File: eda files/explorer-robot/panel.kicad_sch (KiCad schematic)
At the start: 15 parts, among them J11 PANEL.BUS, J12 PANEL.CTRL, U11 TPS22917DBV

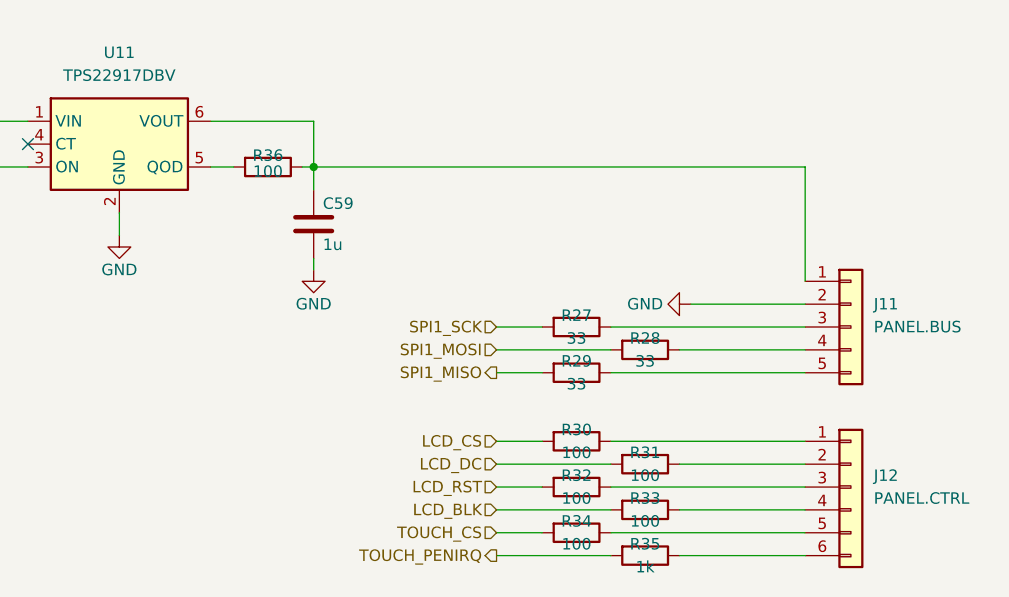
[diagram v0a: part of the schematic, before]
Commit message: ``` Move AI camera branch to 3.3 V rail
The Grove Vision AI V2 module used here requires a 3.3 V input,
so powering it from the switched 5 V branch would over-voltage it.
Point U9 VIN at +3.3V; the TPS22917, footprint and control are
unchanged.

Also bump the 5 V inductor to 15 µH/3 A, swap the catch diode,
clean up schematic wiring and add no-connects on unused pins.
Document the decision in ADR-0025 and update ADR-0019, ADR-0021
and CONTEXT.md.
```
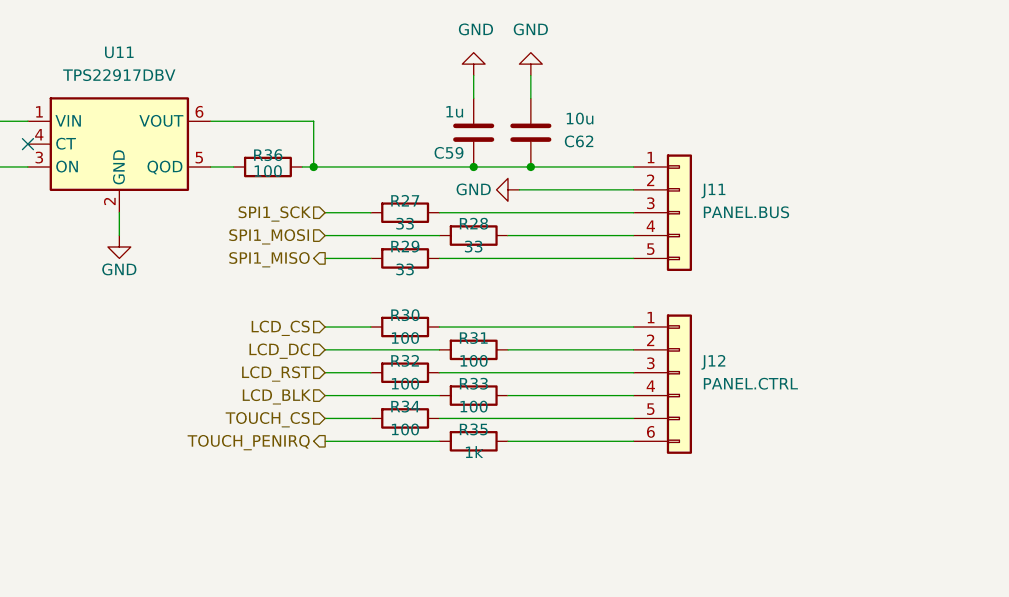
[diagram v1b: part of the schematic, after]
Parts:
- added C62: 10u, Capacitor_SMD:C_0805_2012Metric, symbol Device:C
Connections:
- net GND: now also C62.2
- net at C59.1, J11.1 (Pin_1), R36.1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: now also C62.1
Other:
- moved on the sheet: J11, J12, R27, R28, R29, R30, R31, R32, R33, R34, R35

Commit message: place test points, tidy up, ERC
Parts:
- added TP20: T.TCH.PEN, Connector_PinHeader_2.54mm:PinHeader_1x02_P2.54mm_Vertical, symbol Connector:TestPoint_2Pole
- added TP21: T.TCH.CS, Connector_PinHeader_2.54mm:PinHeader_1x02_P2.54mm_Vertical, symbol Connector:TestPoint_2Pole
- added TP22: T.LCD.CS, Connector_PinHeader_2.54mm:PinHeader_1x02_P2.54mm_Vertical, symbol Connector:TestPoint_2Pole
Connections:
- net GND: now also TP20.1, TP21.1, TP22.1
- net LCD_CS: now also TP22.2
- net TOUCH_CS: now also TP21.2
- net TOUCH_PENIRQ: now also TP20.2
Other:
- note added: "Test Points"

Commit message: Add LCSC part metadata to explorer-robot schematics
Populate JLCPCB_URL, LCSC, MPN, and MFR fields on components in the
panel and rangefinder sheets, and default the BOM view to sort by
LCSC ascending. Rename TB6612FNG test points to match motor encoder
nets, adjust their placement, and drop two symbols from the BOM and
position files.
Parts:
- R27, R28, R29: JLCPCB_URL (none) -> https://jlcpcb.com/partdetail/23867-0603WAF330JT5E/C23140; LCSC (none) -> C23140; MPN (none) -> 0603WAF330JT5E
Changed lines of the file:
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@@
+			)
+		)
+		(property "JLCPCB_URL" "https://jlcpcb.com/partdetail/23867-0603WAF330JT5E/C23140"
+			(at 157.48 85.09 90)
+			(hide yes)
+			(show_name no)
+			(do_not_autoplace no)
+			(effects
+				(font
+					(size 1.27 1.27)
+				)
+			)
+		)
+		(property "LCSC" "C23140"
+			(at 157.48 85.09 90)
+			(hide yes)
+			(show_name no)
+			(do_not_autoplace no)
+			(effects
+				(font
+					(size 1.27 1.27)
+				)
+			)
+		)
+		(property "MPN" "0603WAF330JT5E"
+			(at 157.48 85.09 90)
+			(hide yes)
+			(show_name no)
+			(do_not_autoplace no)
+			(effects
+				(font
+					(size 1.27 1.27)
+				)
 			)
 		)
@@
 			)
 		)
+		(property "JLCPCB_URL" "https://jlcpcb.com/partdetail/23867-0603WAF330JT5E/C23140"
+			(at 149.86 82.55 90)
+			(hide yes)
+			(show_name no)
+			(do_not_autoplace no)
+			(effects
+				(font
+					(size 1.27 1.27)
+				)
+			)
+		)
+		(property "LCSC" "C23140"
+			(at 149.86 82.55 90)
+			(hide yes)
+			(show_name no)
+			(do_not_autoplace no)
+			(effects
+				(font
+					(size 1.27 1.27)
+				)
+			)
+		)
+		(property "MPN" "0603WAF330JT5E"
+			(at 149.86 82.55 90)
+			(hide yes)
+			(show_name no)
+			(do_not_autoplace no)
+			(effects
+				(font
+					(size 1.27 1.27)
+				)
+			)
+		)
 		(pin "1"
 		)
@@
 			(hide yes)
 			(show_name no)
+			(do_not_autoplace no)
+			(effects
+				(font
+					(size 1.27 1.27)
+				)
+			)
+		)
+		(property "JLCPCB_URL" "https://jlcpcb.com/partdetail/23867-0603WAF330JT5E/C23140"
+			(at 149.86 87.63 90)
+			(hide yes)
+			(show_name no)
+			(do_not_autoplace no)
+			(effects
+				(font
+					(size 1.27 1.27)
+				)
+			)
+		)
+		(property "LCSC" "C23140"
+			(at 149.86 87.63 90)
+			(hide yes)
+			(show_name no)
+			(do_not_autoplace no)
+			(effects
+				(font
+					(size 1.27 1.27)
+				)
+			)
+		)
+		(property "MPN" "0603WAF330JT5E"
+			(at 149.86 87.63 90)
+			(hide yes)
+			(show_name no)

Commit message: Update AI camera branch to 5V and document schematic
- ADR-0027 supersedes ADR-0025: AI camera input is 5V, not 3.3V
- Move U9 VIN and C55 back to +5V in aicam.kicad_sch
- Update CONTEXT.md branch descriptions and ADR cross-references
- Record ICM-20948 placement status and corrected battery divider ratio
- Adjust battery_charge_read for 33k/10k divider (0.2326 ratio)
- Enable sheet component classes; refresh netlist and PCB footprints
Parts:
- R27, R28, R29: MFR (none) -> UNI-ROYAL(Uniroyal Elec)
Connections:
- net +5V: now also C58.1
- net PANEL_PWR: no longer C58.1

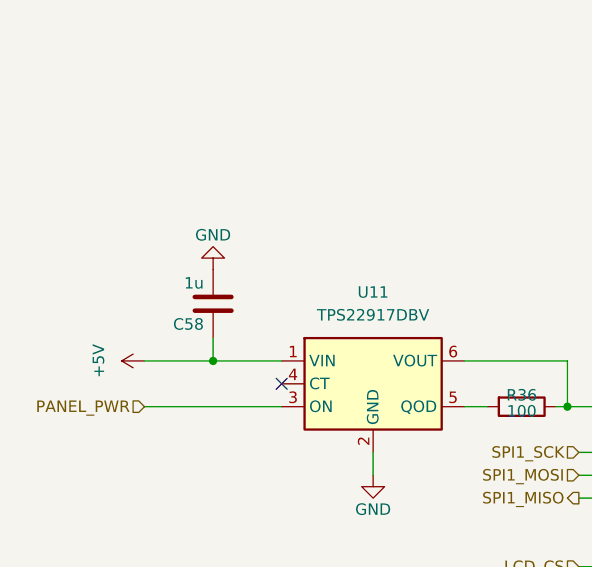
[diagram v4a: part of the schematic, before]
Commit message: Add 1 nF CT capacitors to TPS22917 load switches
Specify C29/C30/C67/C68 on the LiDAR, AI camera, expansion and
panel branches to give a controlled rise and limit inrush. Update
ADRs 0010, 0021, 0024 and 0027 and CONTEXT.md to match, rework the
affected schematics, and swap the inductor footprint to the
EasyEDA SLO0618H part.
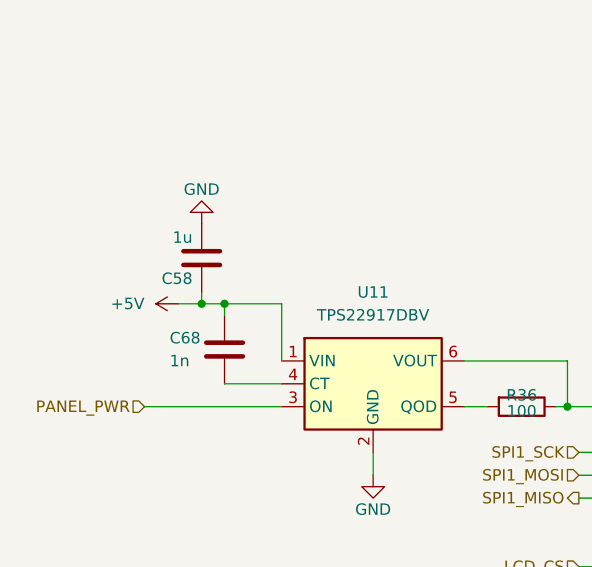
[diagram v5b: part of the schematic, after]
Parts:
- added C68: 1n, Capacitor_SMD:C_0603_1608Metric, symbol Device:C
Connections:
- net +5V: now also C68.2
- net at U11.4 (CT): now also C68.1
- no-connect marks 1 -> 0
